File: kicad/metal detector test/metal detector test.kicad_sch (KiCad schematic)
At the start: 81 parts, among them J1 AudioJack3_SwitchT, SW0 SW_SPST, SW1 SW_SPST, SW2 SW_SPST, SW3 SW_SPST, SW4 SW_SPST, SW5 SW_SPST, SW6 SW_SPST, SW7 SW_SPST, SW8 SW_SPST, U1 UA78M05CDCYRG3, U10 LS20-S, U2 OPA2320AID, U3 LT1129CST-3.3#PBF, U4 UA78M05CDCYRG3, U5 LM2940IMP-9.0/NOPB, U6 OPA2140AID, U7 MAX7423EUA+, U8 MAX7423EUA+, U9 LT1129CST-3.3#PBF

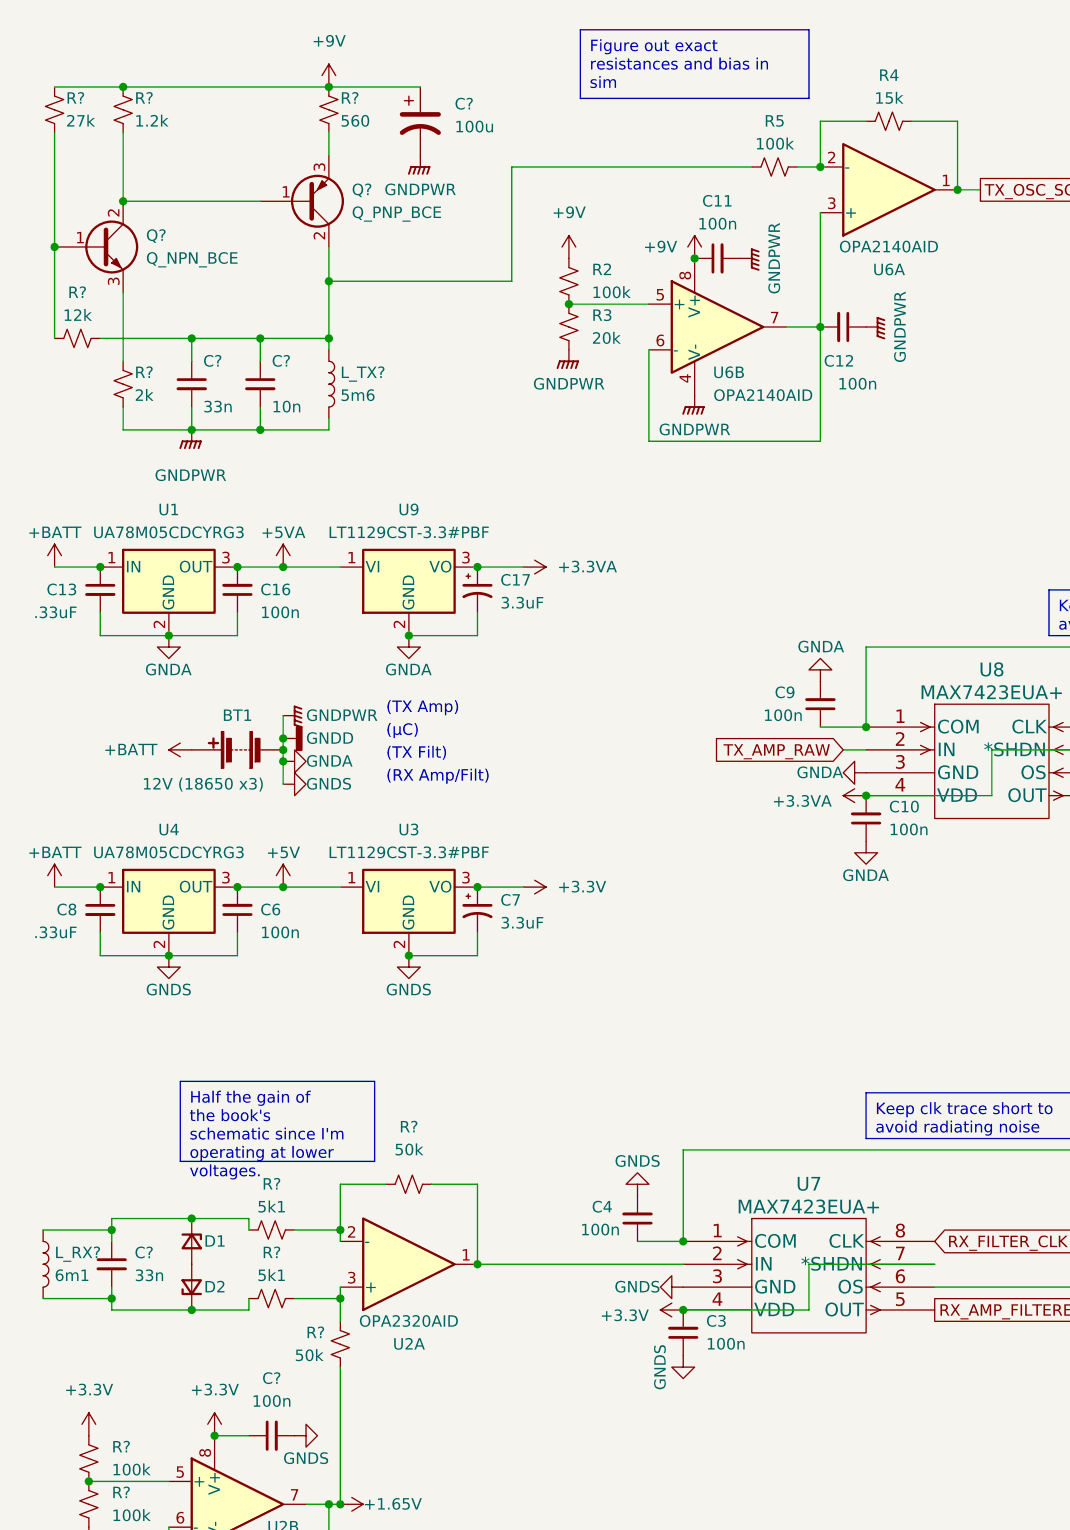
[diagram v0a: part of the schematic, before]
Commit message: Realized the rx op amp has a built in limiter so no need for the external zeners, plus they apparently create a significant temperature-dependent offset voltage so that's not great.
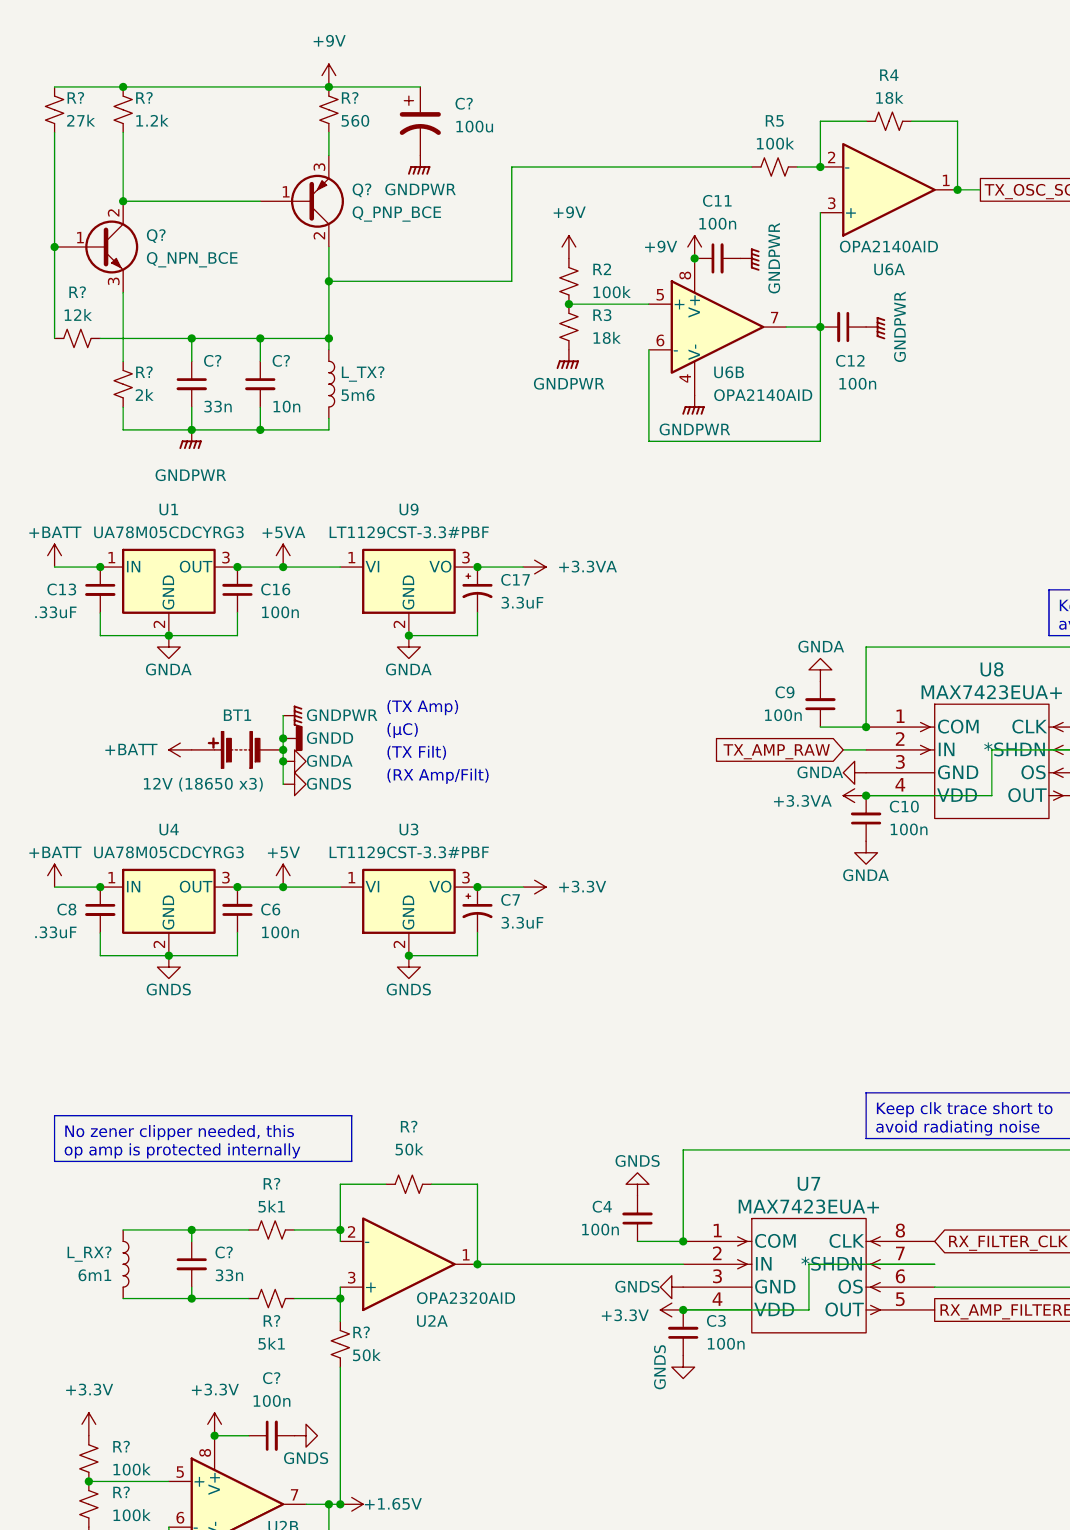
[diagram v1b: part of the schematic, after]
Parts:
- removed D1, D2: D_Zener_Small, symbol Device:D_Zener_Small
- OLED?: footprint (none) -> Connector_PinHeader_2.54mm:PinHeader_1x07_P2.54mm_Vertical
- R3: value 20k -> 18k
- R4: value 15k -> 18k
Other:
- moved on the sheet: C?, L_RX?

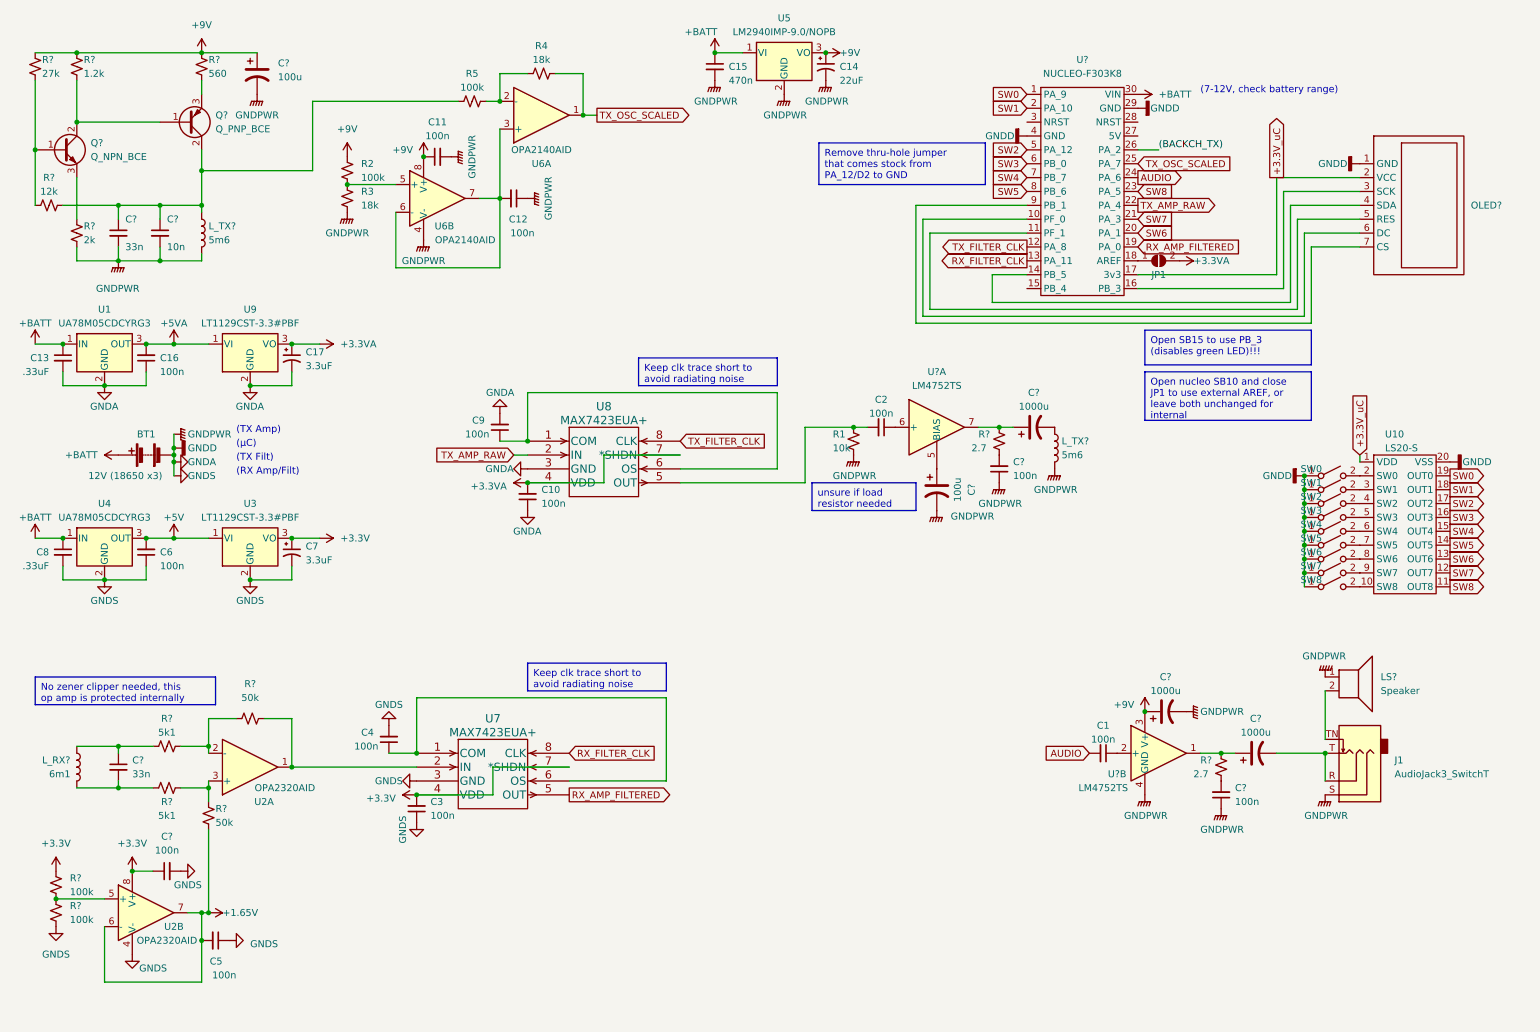
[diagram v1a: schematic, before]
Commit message: Added battery voltage measurement and a big cap on the battery input
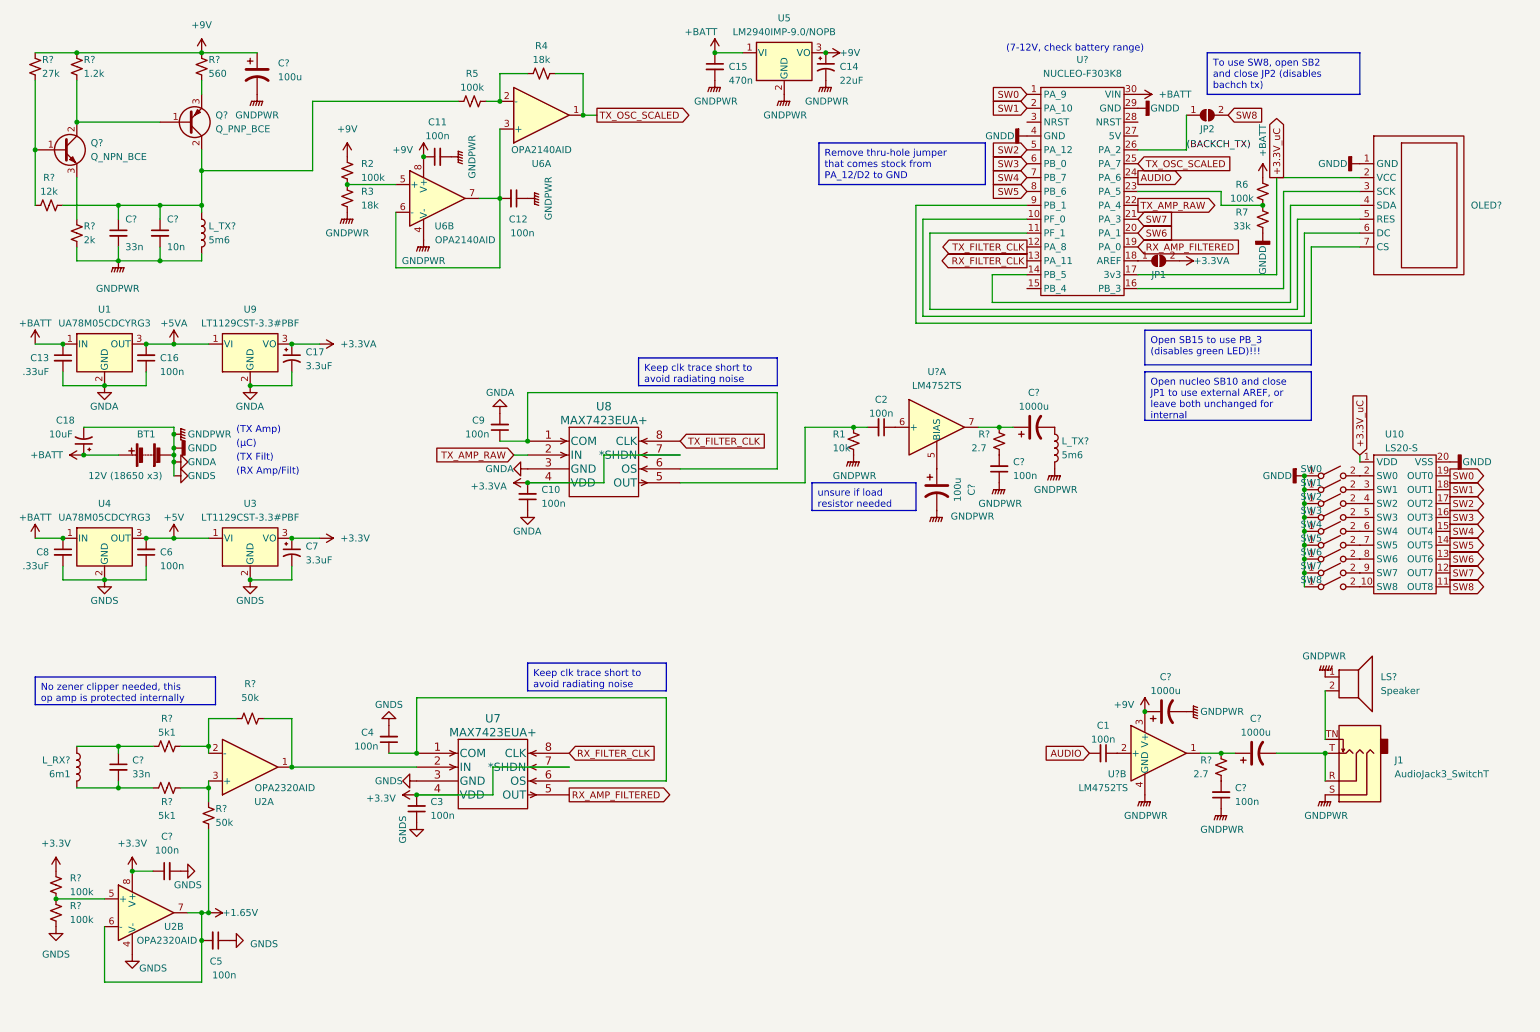
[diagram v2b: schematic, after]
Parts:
- added C18: 10uF, Capacitor_SMD:C_0805_2012Metric_Pad1.18x1.45mm_HandSolder, symbol Device:C_Polarized_Small_US
- added JP2: SolderJumper_2_Open, Jumper:SolderJumper-2_P1.3mm_Open_Pad1.0x1.5mm, symbol Jumper:SolderJumper_2_Open
- added R6: 100k, Resistor_SMD:R_0805_2012Metric_Pad1.20x1.40mm_HandSolder, symbol Device:R_Small_US
- added R7: 33k, Resistor_SMD:R_0805_2012Metric_Pad1.20x1.40mm_HandSolder, symbol Device:R_Small_US
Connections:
- net (BACKCH_TX): now also JP2.1 (A)
- net +BATT: now also C18.1, R6.1
- net GNDA: now also C18.2, R7.2
- net SW8: now also JP2.2 (B); no longer U?.23 (PA_5)
- new net: R6.2, R7.1, U?.23 (PA_5)

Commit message: Added smt ferrite bead and cap to gnd on oled power input since amazon review reported that it's noise bleeds back into the uC, also made power for it optionally come from 5v or 3.3v with solder jumpers... I suspect the 5v may be better since if it gets noise it will be reduced by the nucleo 3.3v regulator's psrr.
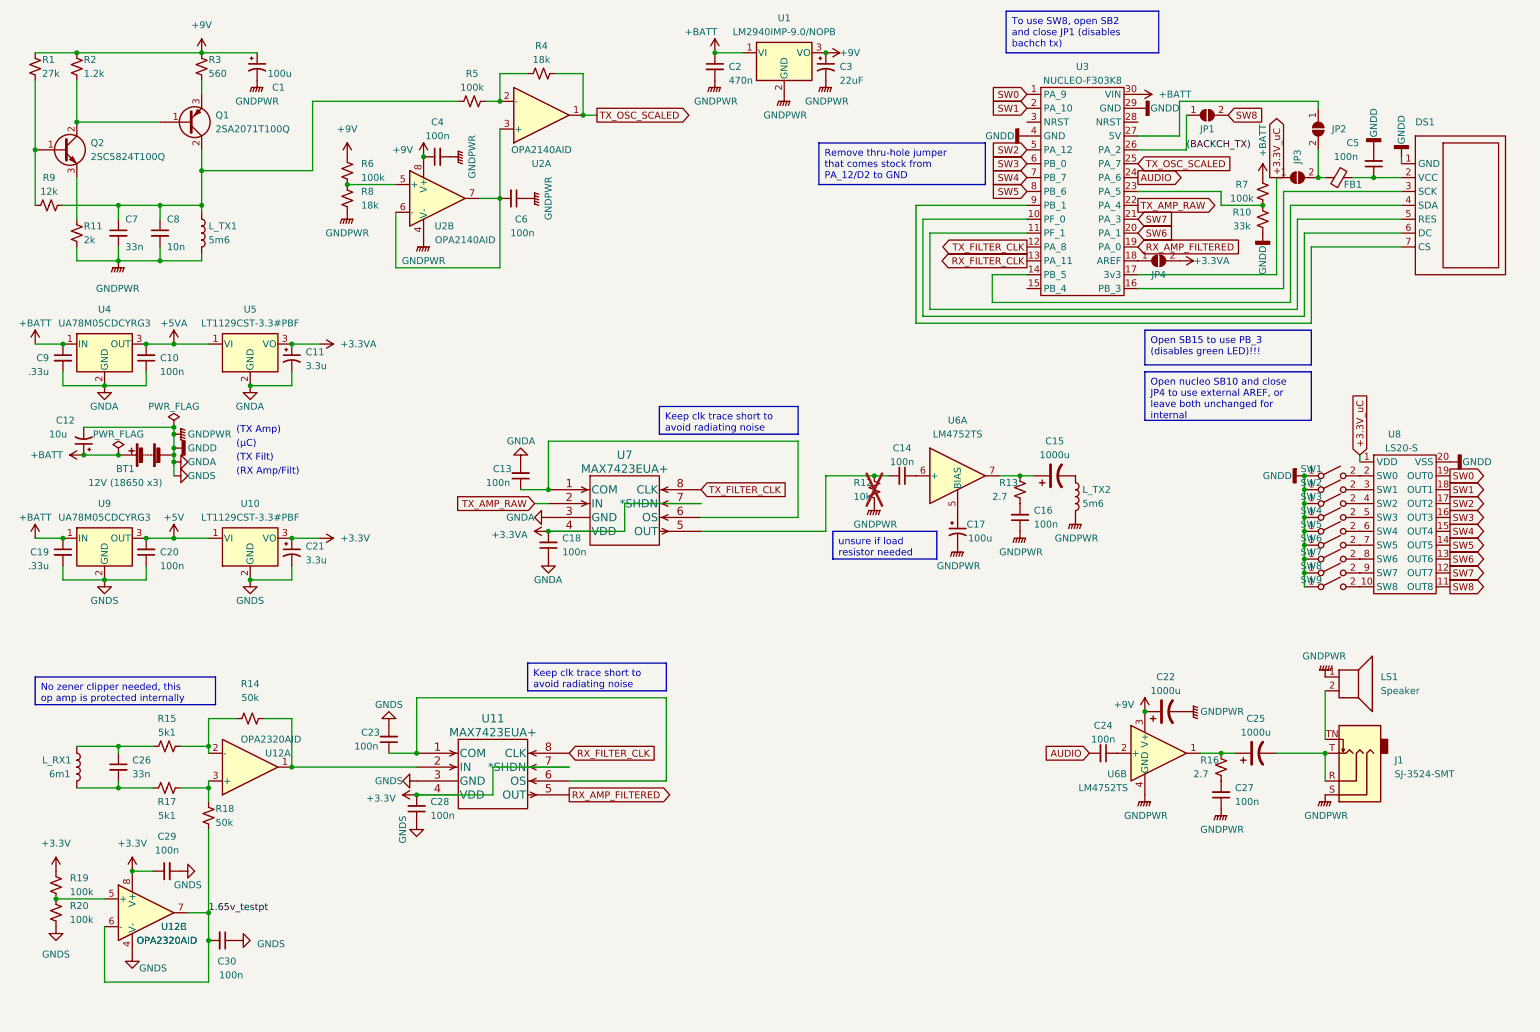
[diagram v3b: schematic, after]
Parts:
- removed C? (x2): 100u, Capacitor_SMD:CP_Elec_5x5.9, symbol Device:C_Polarized_US
- removed C? (x2): 1000u, Capacitor_SMD:CP_Elec_5x5.9, symbol Device:C_Polarized_US
- removed OLED?: 2.42_inch_128x64_oled, Connector_PinHeader_2.54mm:PinHeader_1x07_P2.54mm_Vertical, symbol oled_allen:2.42_inch_128x64_oled
- removed U?: NUCLEO-F303K8, symbol stm32_allen:NUCLEO-F303K8
- added C1, C17: 100u, Capacitor_SMD:C_1206_3216Metric_Pad1.33x1.80mm_HandSolder, symbol Device:C_Polarized_Small_US
- added C22, C25: 1000u, Capacitor_THT:CP_Radial_D10.0mm_P5.00mm, symbol Device:C_Polarized_US
- added C5: 100n, Capacitor_SMD:C_0805_2012Metric_Pad1.18x1.45mm_HandSolder, symbol Device:C_Small
- added DS1: 2.42_inch_128x64_oled, symbol allen_oled:2.42_inch_128x64_oled
- added FB1: FerriteBead_Small, Inductor_SMD:L_0805_2012Metric_Pad1.05x1.20mm_HandSolder, symbol Device:FerriteBead_Small
- added JP2, JP3: SolderJumper_2_Open, Jumper:SolderJumper-2_P1.3mm_Open_Pad1.0x1.5mm, symbol Jumper:SolderJumper_2_Open
- added U3: NUCLEO-F303K8, symbol allen_stm32:NUCLEO-F303K8
- BT1: footprint (none) -> Connector_PinHeader_2.54mm:PinHeader_1x02_P2.54mm_Vertical
- C11: renamed from C17; value 3.3uF -> 3.3u
- C12: renamed from C18; value 10uF -> 10u; footprint Capacitor_SMD:C_0805_2012Metric_Pad1.18x1.45mm_HandSolder -> Capacitor_SMD:C_1206_3216Metric_Pad1.33x1.80mm_HandSolder
- C15: renamed from C?; footprint Capacitor_SMD:CP_Elec_5x5.9 -> Capacitor_THT:CP_Radial_D10.0mm_P5.00mm
- C19: renamed from C8; value .33uF -> .33u
- C21: renamed from C7; value 3.3uF -> 3.3u
- C9: renamed from C13; value .33uF -> .33u
- J1: value AudioJack3_SwitchT -> SJ-3524-SMT; footprint (none) -> allen footprints:SJ-3524-SMT_audio_jack_with_tip_switch_smt
- Q1: renamed from Q?; value Q_PNP_BCE -> 2SA2071T100Q
- Q2: renamed from Q?; value Q_NPN_BCE -> 2SC5824T100Q
- R12: renamed from R1; now not fitted
- gave numbers to parts that had none: 24
- renumbered C16 to C10, C9 to C13, C2 to C14, C10 to C18, C15 to C2, C6 to C20, C4 to C23, C1 to C24, C3 to C28, C14 to C3, C5 to C30, C11 to C4, C12 to C6, JP2 to JP1, JP1 to JP4, R7 to R10, R2 to R6, R6 to R7, R3 to R8, SW0 to SW1, SW1 to SW2, SW2 to SW3, SW3 to SW4, SW4 to SW5, SW5 to SW6, SW6 to SW7, SW7 to SW8, SW8 to SW9, U5 to U1, U3 to U10, U7 to U11, U2 to U12, U6 to U2, U1 to U4, U9 to U5, U8 to U7, U10 to U8, U4 to U9
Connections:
- net (BACKCH_TX): now also U3.26 (PA_2)
- net +3.3V_uC: now also JP3.1 (A), U3.17 (3v3)
- net +9V: now also C1.1, C22.1
- net +BATT: now also U3.30 (VIN)
- net AUDIO: now also U3.24 (PA_6)
- net GNDA: now also C1.2, C17.2, C22.2, C5.2, DS1.1 (GND), U3.29 (GND), U3.4 (GND)
- net RX_AMP_FILTERED: now also U3.19 (PA_0)
- net RX_FILTER_CLK: now also U3.13 (PA_11)
- net SW0: now also U3.1 (PA_9)
- net SW1: now also U3.2 (PA_10)
- net SW2: now also U3.5 (PA_12)
- net SW3: now also U3.6 (PB_0)
- net SW4: now also U3.7 (PB_7)
- net SW5: now also U3.8 (PB_6)
- net SW6: now also U3.20 (PA_1)
- net SW7: now also U3.21 (PA_3)
- net TX_AMP_RAW: now also U3.22 (PA_4)
- net TX_FILTER_CLK: now also U3.12 (PA_8)
- net TX_OSC_SCALED: now also U3.25 (PA_7)
- net at U6.5 (BIAS): now also C17.1
- net at R16.1, U6.1: now also C25.1
- net at J1.R, J1.T: now also C25.2
- net at JP4.1 (A): now also U3.18 (AREF)
- net at R10.1, R7.2: now also U3.23 (PA_5)
- net +1.65V renamed 1.65v_testpt
- new net: FB1.1, JP2.2 (B), JP3.2 (B)
- new net: C5.1, DS1.2 (VCC), FB1.2
- new net: DS1.3 (SCK), U3.16 (PB_3)
- new net: DS1.4 (SDA), U3.14 (PB_5)
- new net: DS1.5 (RES), U3.11 (PF_1)
- new net: DS1.6 (DC), U3.10 (PF_0)
- new net: DS1.7 (CS), U3.9 (PB_1)
- new net: JP2.1 (A), U3.27 (5V)
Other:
- note removed: "(7-12V, check battery range)"
- moved on the sheet: C13, C14, C15, C16, C18, C30, L_TX2, R13, U6A, U7
